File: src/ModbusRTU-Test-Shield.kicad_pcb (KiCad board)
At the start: 2 copper layers, 68.6 x 53.3 mm, 46 parts, among them J1 SP-140520-08-001, J2 SP-140520-10-001, J3 SP-140520-08-001, J4 SP-140520-06-001, J5 5430438, J6 54601-906WPLF, SW1 BUTTON1, SW2 BUTTON2, SW3 RESET, SW4 OS202011MS2QN1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

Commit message: Made some changes based on build.
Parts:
- R1, R2, R3, R4, R5, R6, R7, R8: value 330 -> 1K
- REF**: footprint Symbol:KiCad-Logo2_5mm_SilkScreen -> Project_Footprints:KiCad-Logo2_5mm_SilkScreen
- REF**: footprint Symbol:OSHW-Logo_7.5x8mm_SilkScreen -> Project_Footprints:OSHW-Logo_7.5x8mm_SilkScreen
- moved REF** 40.4 mm to (118.7, 112.4)
- moved D5 13.3 mm to (154.9, 122.6)
- moved D6 13.3 mm to (154.9, 116.2)
- moved D7 13.3 mm to (154.9, 109.9)
- moved D8 13.3 mm to (154.9, 103.5)
- moved D1 13.3 mm to (161.3, 122.6)
- moved D2 13.3 mm to (161.3, 116.2)
- moved D3 13.3 mm to (161.3, 109.9)
- moved D4 13.3 mm to (161.3, 103.5)
- moved RV1 12.8 mm to (144.8, 120.7)
- moved RV2 12.8 mm to (144.8, 105.4)
- moved REF** 2.62 mm to (141.0, 126.4)
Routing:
- net +5V: track 101.1 -> 122.6 mm
- net /IOREF: track 91.2 -> 70.9 mm
- net Net-(D7-K): track 15.5 -> 23.1 mm
- net Net-(D1-A): track 33.8 -> 26.3 mm
- net /POT1: track 14.2 -> 21.2 mm
- net /POT2: track 28.6 -> 34.5 mm
- net Net-(D2-A): track 25.3 -> 20.5 mm
- net Net-(D5-K): track 32.5 -> 29.3 mm
- net Net-(D3-A): track 16.8 -> 14.7 mm
- net Net-(D8-K): track 8.08 -> 9.99 mm
- net Net-(D4-A): track 9.35 -> 8.72 mm

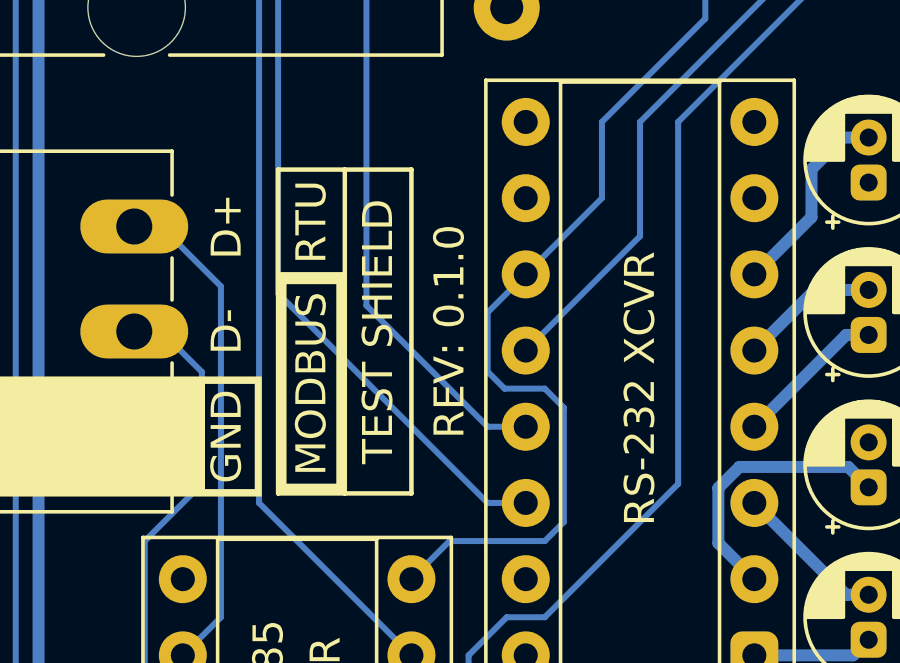
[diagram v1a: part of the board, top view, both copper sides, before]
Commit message: Updated board to 1.0.0. Changed out RJ12 connector for one that is not obsolete. Changed out RS-485 tranceiver for a less expensive model.
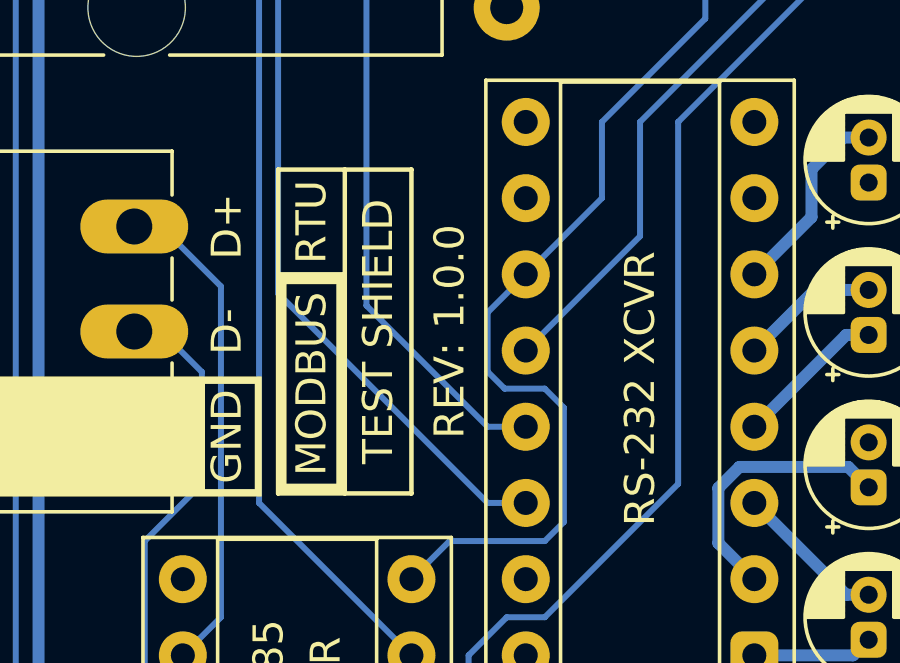
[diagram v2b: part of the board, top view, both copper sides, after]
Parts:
- J6: value 54601-906WPLF -> RJ12 CONNECTOR
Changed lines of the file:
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@@
   (title_block
     (title "ModbusRTU Test Shield")
-    (date "2024-01-06")
-    (rev "0.1.0")
+    (date "2024-11-29")
+    (rev "1.0.0")
     (company "Designer: C. M. Bulliner")
     (comment 2 "OF MERCHANTABILITY, SATISFACTORY QUALITY AND FITNESS FOR A PARTICULAR PURPOSE.")
@@
     (tags "THT DIP DIL PDIP 2.54mm 7.62mm 300mil Socket")
     (property "Description" "RS-485 Half-Duplex Transceiver")
-    (property "Manufacturer" "Analog Devices")
-    (property "Part Number" "LT1785ACN8#PBF")
+    (property "Manufacturer" "Texas Instruments")
+    (property "Part Number" "SN65HVD3082EP")
     (property "Sheetfile" "ModbusRTU-Test-Shield.kicad_sch")
     (property "Sheetname" "")
@@
     (property "Description" "RJ12 Connector")
     (property "Manufacturer" "Amphenol ICC (FCI)")
-    (property "Part Number" "54601-906WPLF")
+    (property "Part Number" "87180-066LF")
     (property "Sheetfile" "ModbusRTU-Test-Shield.kicad_sch")
     (property "Sheetname" "")
@@
     (property "ki_keywords" "6P6C RJ socket connector")
     (attr through_hole)
-    (fp_text reference "J6" (at 0 -8.1 180) (layer "F.Fab")
-        (effects (font (size 1 1) (thickness 0.15)))
-    )
-    (fp_text value "54601-906WPLF" (at 0 3.175 90) (layer "F.Fab") hide
+    (fp_text reference "J6" (at 0 -8.1) (layer "F.Fab")
+        (effects (font (size 1 1) (thickness 0.15)))
+    )
+    (fp_text value "RJ12 CONNECTOR" (at 0 3.175 90) (layer "F.Fab") hide
         (effects (font (size 1 1) (thickness 0.15)))
     )
@@
     (pad "6" thru_hole circle locked (at 3.18 -12.43 270) (size 1.52 1.52) (drill 0.76) (layers "*.Cu" "*.Mask")
       (net 1 "GND") (pintype "passive"))
-    (model "${KIPRJMOD}/project_libraries/Project_3DModels.3dshapes/FCI_54601-906WPLF.step"
-      (offset (xyz 0 -1.8 0))
+    (model "${KIPRJMOD}/project_libraries/Project_3DModels.3dshapes/AmphenolFCI_87180-x66lf.step"
+      (offset (xyz 0 -1.8 11.5))
       (scale (xyz 1 1 1))
       (rotate (xyz -90 0 0))
